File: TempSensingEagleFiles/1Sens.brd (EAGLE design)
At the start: 34.5 x 34 mm, 6 parts, among them U3 MLX90614_

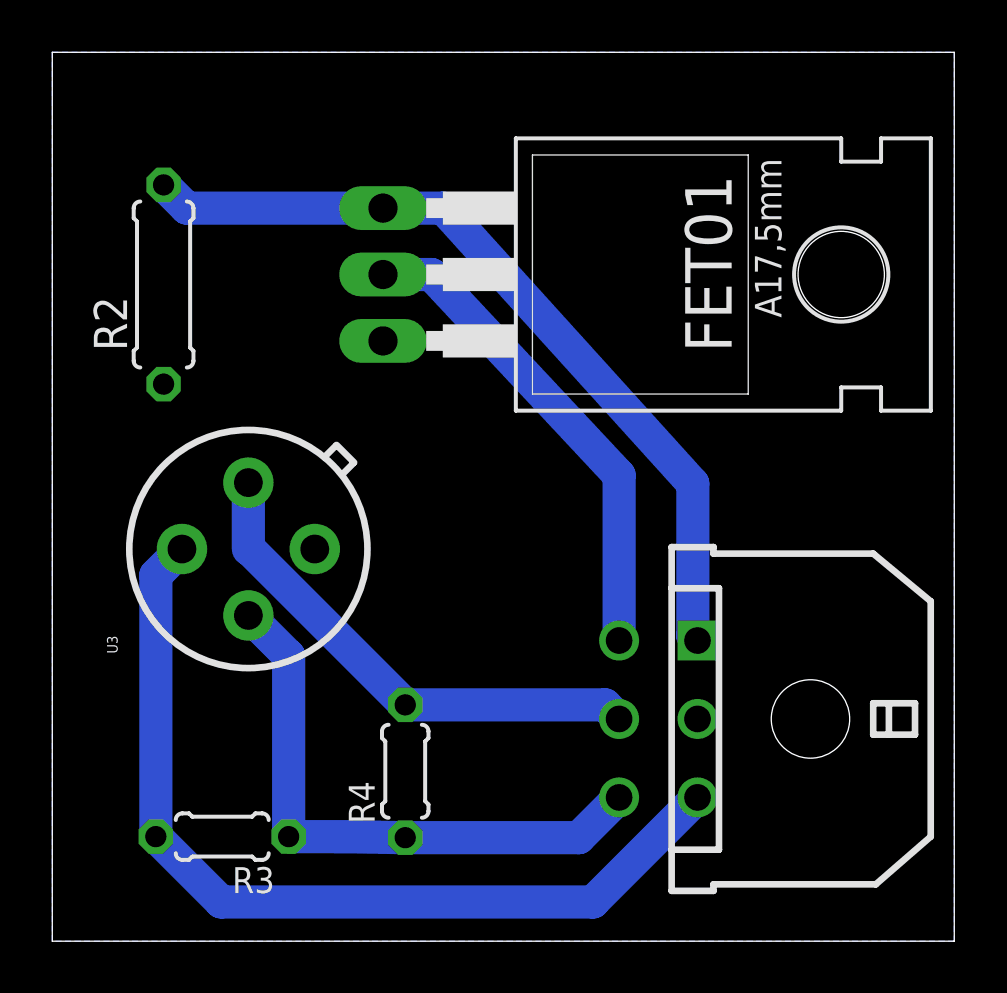
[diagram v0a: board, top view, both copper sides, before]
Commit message: STABLE: working with only one sensor
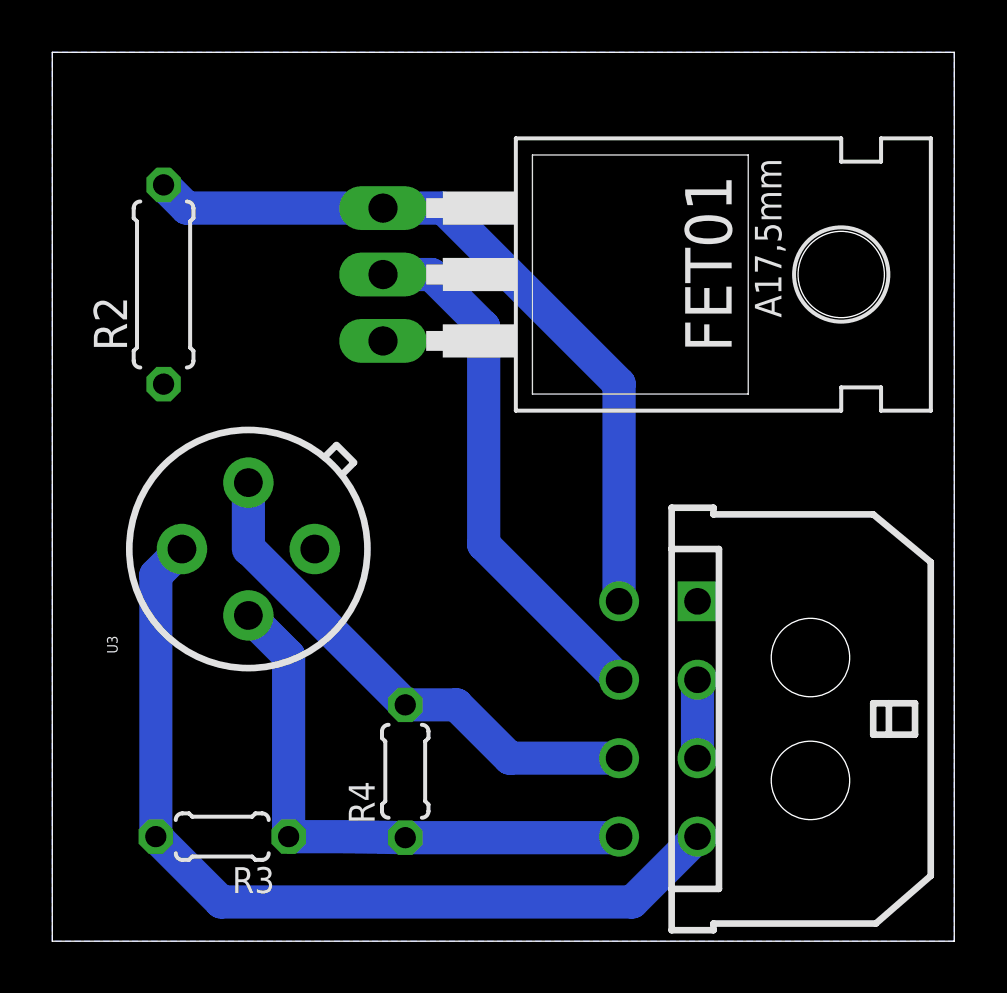
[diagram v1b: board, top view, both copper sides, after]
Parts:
- JP1: device con-molex-micro-fit-3_0:43045-0600 -> con-molex-micro-fit-3_0:43045-0800
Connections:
- new net +9V: JP1.P$2, JP1.P$3
- net GND: now also JP1.P$1; no longer JP1.P$2
- net N$1: now also JP1.P$8; no longer JP1.P$6
- net N$15: now also JP1.P$7; no longer JP1.P$5
- net N$16: now also JP1.P$4; no longer JP1.P$3
- net N$18: now also JP1.P$5; no longer JP1.P$1
- net N$2: now also JP1.P$6; no longer JP1.P$4
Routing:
- net +9V: track 0.00 -> 3.00 mm
- net N$18: track 31.4 -> 28.9 mm
- net N$2: track 18.7 -> 20.3 mm
- net N$16: track 34.8 -> 34.2 mm
- net N$1: track 22.4 -> 21.8 mm
- net N$15: track 19.4 -> 20.0 mm
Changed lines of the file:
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@@
 <wire x1="34.5" y1="34" x2="0" y2="34" width="0" layer="20"/>
 <wire x1="0" y1="34" x2="0" y2="0" width="0" layer="20"/>
-<text x="19.5" y="11.5" size="0.6096" layer="110">vib</text>
-<text x="19.5" y="9" size="0.6096" layer="110">scl</text>
-<text x="28" y="8.5" size="0.6096" layer="110" rot="R180">GND</text>
-<text x="28" y="5.5" size="0.6096" layer="110" rot="R180">SDA</text>
-<text x="20.5" y="6" size="0.6096" layer="110" rot="R180">VCC ioio</text>
-<text x="27.5" y="12.5" size="0.6096" layer="110" rot="R180">ioio
+<text x="19.5" y="9.5" size="0.6096" layer="110">vib</text>
+<text x="19.5" y="6.5" size="0.6096" layer="110">scl</text>
+<text x="28" y="13.5" size="0.6096" layer="110" rot="R180">GND</text>
+<text x="28" y="4" size="0.6096" layer="110" rot="R180">SDA</text>
+<text x="20.5" y="4" size="0.6096" layer="110" rot="R180">VCC ioio</text>
+<text x="20.5" y="13.5" size="0.6096" layer="110" rot="R180">ioio
 pin</text>
 </plain>
@@
 <element name="R4" library="rcl" package="0204/5" value="4.1k" x="13.5" y="6.5" rot="R90"/>
 <element name="R3" library="rcl" package="0204/5" value="4.1k" x="6.5" y="4" rot="R180"/>
-<element name="JP1" library="con-molex-micro-fit-3_0" package="43045-0600" value="" x="29" y="8.5" rot="R90"/>
+<element name="JP1" library="con-molex-micro-fit-3_0" package="43045-0800" value="" x="29" y="8.5" rot="R90"/>
 </elements>
 <signals>
@@
 <wire x1="7.5" y1="15" x2="7.54" y2="15" width="0.8128" layer="16"/>
 <wire x1="7.54" y1="15" x2="13.5" y2="9.04" width="1.27" layer="16"/>
-<contactref element="JP1" pad="P$5"/>
-<wire x1="13.5" y1="9.04" x2="21.14" y2="9.04" width="1.27" layer="16"/>
-<wire x1="21.14" y1="9.04" x2="21.68" y2="8.5" width="1.27" layer="16"/>
+<contactref element="JP1" pad="P$7"/>
+<wire x1="13.5" y1="9.04" x2="15.46" y2="9.04" width="1.27" layer="16"/>
+<wire x1="15.46" y1="9.04" x2="17.5" y2="7" width="1.27" layer="16"/>
+<wire x1="17.5" y1="7" x2="21.68" y2="7" width="1.27" layer="16"/>
 </signal>
 <signal name="N$16">
@@
 <wire x1="3.96" y1="4" x2="3.96" y2="14" width="1.27" layer="16"/>
 <wire x1="3.96" y1="14" x2="4.96" y2="15" width="1.27" layer="16"/>
-<contactref element="JP1" pad="P$3"/>
 <wire x1="3.96" y1="4" x2="6.46" y2="1.5" width="1.27" layer="16"/>
-<wire x1="6.46" y1="1.5" x2="20.68" y2="1.5" width="1.27" layer="16"/>
-<wire x1="20.68" y1="1.5" x2="24.68" y2="5.5" width="1.27" layer="16"/>
+<wire x1="6.46" y1="1.5" x2="22.18" y2="1.5" width="1.27" layer="16"/>
+<contactref element="JP1" pad="P$4"/>
+<wire x1="22.18" y1="1.5" x2="24.68" y2="4" width="1.27" layer="16"/>
 </signal>
 <signal name="N$18">
@@
 <wire x1="4.2564" y1="28.9278" x2="5.1442" y2="28.04" width="1.27" layer="16"/>
 <wire x1="5.1442" y1="28.04" x2="12.65" y2="28.04" width="1.27" layer="16"/>
-<contactref element="JP1" pad="P$1"/>
 <wire x1="12.65" y1="28.04" x2="14.96" y2="28.04" width="1.27" layer="16"/>
-<wire x1="14.96" y1="28.04" x2="24.5" y2="17.5" width="1.27" layer="16"/>
-<wire x1="24.5" y1="17.5" x2="24.5" y2="11.68" width="1.27" layer="16"/>
-<wire x1="24.5" y1="11.68" x2="24.68" y2="11.5" width="1.27" layer="16"/>
+<contactref element="JP1" pad="P$5"/>
+<wire x1="14.96" y1="28.04" x2="21.68" y2="21.32" width="1.27" layer="16"/>
+<wire x1="21.68" y1="21.32" x2="21.68" y2="13" width="1.27" layer="16"/>
 </signal>
 <signal name="N$1">
@@
 <wire x1="9.04" y1="4" x2="9.04" y2="10.92" width="1.27" layer="16"/>
 <wire x1="9.04" y1="10.92" x2="7.5" y2="12.46" width="1.27" layer="16"/>
-<contactref element="JP1" pad="P$6"/>
-<wire x1="13.5" y1="3.96" x2="20.14" y2="3.96" width="1.27" layer="16"/>
-<wire x1="20.14" y1="3.96" x2="21.68" y2="5.5" width="1.27" layer="16"/>
+<wire x1="13.5" y1="3.96" x2="21.64" y2="3.96" width="1.27" layer="16"/>
+<contactref element="JP1" pad="P$8"/>
+<wire x1="21.64" y1="3.96" x2="21.68" y2="4" width="1.27" layer="16"/>
 </signal>
 <signal name="GND">
@@
 <vertex x="0" y="0"/>
 </polygon>
-<contactref element="JP1" pad="P$2"/>
+<contactref element="JP1" pad="P$1"/>
 </signal>
 <signal name="N$2">
 <contactref element="FET01" pad="C"/>
-<contactref element="JP1" pad="P$4"/>
 <wire x1="12.65" y1="25.5" x2="14.5" y2="25.5" width="1.27" layer="16"/>
-<wire x1="14.5" y1="25.5" x2="21.68" y2="17.82" width="1.27" layer="16"/>
-<wire x1="21.68" y1="17.82" x2="21.68" y2="11.5" width="1.27" layer="16"/>
+<contactref element="JP1" pad="P$6"/>
+<wire x1="14.5" y1="25.5" x2="16.5" y2="23.5" width="1.27" layer="16"/>
+<wire x1="16.5" y1="23.5" x2="16.5" y2="15.18" width="1.27" layer="16"/>
+<wire x1="16.5" y1="15.18" x2="21.68" y2="10" width="1.27" layer="16"/>
+</signal>
+<signal name="+9V">
+<contactref element="JP1" pad="P$3"/>
+<contactref element="JP1" pad="P$2"/>
+<wire x1="24.68" y1="10" x2="24.68" y2="7" width="1.27" layer="16"/>
 </signal>
 </signals>
